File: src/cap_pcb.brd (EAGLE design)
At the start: 36 x 80 mm, 8 parts, among them CON1 PINHEAD_2X02-PTH-2-MALE, CON6 PINHEAD_2X02-PTH-2-MALE

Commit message: Updates here and there
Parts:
- removed CON6: PINHEAD_2X02-PTH-2-MALE, pinhead:2X02-PTH-2
- added CON2, CON3, CON4: PINHEAD_2X02-PTH-2-MALE, pinhead:2X02-PTH-2
- C17, C18, C19, C20, C21, C23: value 100µF -> 330µF
- moved C18 28.3 mm to (-8.75, 23.4), turned to 180 degrees
- moved C19 28.3 mm to (8.75, 23.4), turned to 180 degrees
- moved C20 22.5 mm to (-8.75, 47.9), turned to 180 degrees
- moved C21 22.5 mm to (8.75, 47.9), turned to 180 degrees
- moved CON1 1.00 mm to (15.7, 57.0)
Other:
- board size 36 x 80 mm -> 36 x 68 mm

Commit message: capacitor PCB polygons update
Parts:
- added PAD1, PAD2, PAD3, PAD4, PAD5, PAD6, PAD7, PAD8: PAD-5X4, PADS:5X4
- added U$1, U$2: (no value), logo:ZUBAX_25X12
- flipped C17 to the bottom
- flipped C23 to the bottom
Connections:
- net GND: now also CON3.1, CON3.2, CON3.3, CON3.4, CON4.1, CON4.2, CON4.3, CON4.4, PAD3.P$1, PAD6.P$1, PAD7.P$1, PAD8.P$1
- net VBAT: now also CON1.1, CON1.2, CON1.3, CON1.4, CON2.1, CON2.2, CON2.3, CON2.4, PAD1.P$1, PAD2.P$1, PAD4.P$1, PAD5.P$1
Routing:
- added copper zone on layer 16, net GND
- added copper zone on layer 1, net VBAT
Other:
- board size 36 x 68 mm -> 36 x 70 mm
- board text added: "GND"
- board text added: "VDC"

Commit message: Silkscreen updates
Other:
- board text added: "+"
- board text added: "-"
- board text added: "Valenok CAP PCB V0.1"
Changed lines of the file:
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@@
 <setting verticaltext="up"/>
 </settings>
-<grid distance="1" unitdist="mm" unit="mm" style="lines" multiple="1" display="yes" altdistance="5" altunitdist="mil" altunit="mil"/>
+<grid distance="0.5" unitdist="mm" unit="mm" style="lines" multiple="1" display="yes" altdistance="5" altunitdist="mil" altunit="mil"/>
 <layers>
 <layer number="1" name="Top" color="4" fill="1" visible="yes" active="yes"/>
@@
 </layers>
 <board>
-<fusionsync huburn="a.cGVyc29uYWw6dWUyYWE4ZDY4" projecturn="a.cGVyc29uYWw6dWUyYWE4ZDY4IzIwMjAwOTI1MzM2NDYxMjgx" f3durn="urn:adsk.wipprod:dm.lineage:IhySjAM5SyGK940RRZt57A" pcbguid="" lastpulledtime="" lastsyncedchangeguid="" latestrevisionid="afba331b-8359-4740-9163-e93e92381942" lastsyncedrevisionid="afba331b-8359-4740-9163-e93e92381942" lastboardhashguid="2d678b6d-4d74-7ef4-afec-71a2cf9df9c4" lastpushedtime="2020-10-31T23:32:12Z" linktopcb3d="true"/>
+<fusionsync huburn="a.cGVyc29uYWw6dWUyYWE4ZDY4" projecturn="a.cGVyc29uYWw6dWUyYWE4ZDY4IzIwMjAwOTI1MzM2NDYxMjgx" f3durn="urn:adsk.wipprod:dm.lineage:IhySjAM5SyGK940RRZt57A" pcbguid="" lastpulledtime="" lastsyncedchangeguid="" latestrevisionid="b7570ab4-b679-4fac-b5e5-818cc3172e16" lastsyncedrevisionid="b7570ab4-b679-4fac-b5e5-818cc3172e16" lastboardhashguid="ee9d795c-402e-5159-a8c4-1897fa97820f" lastpushedtime="2020-11-16T10:37:36Z" linktopcb3d="true"/>
 <plain>
 <wire x1="0" y1="0" x2="0" y2="80" width="0.01" layer="47" style="shortdash" locked="yes"/>
@@
 <text x="15" y="18" size="2" layer="22" font="vector" ratio="15" rot="MR0" align="center">VDC</text>
 <text x="-15" y="18" size="2" layer="22" font="vector" ratio="15" rot="MR0" align="center">GND</text>
+<text x="-16" y="38" size="2.3" layer="21" font="vector" ratio="15" rot="R90" align="center">Valenok CAP PCB V0.1</text>
+<text x="-5" y="51" size="2.3" layer="21" font="vector" ratio="15" align="center">+</text>
+<text x="-5" y="49" size="2.3" layer="21" font="vector" ratio="15" align="center">+</text>
+<text x="13" y="50" size="2.3" layer="21" font="vector" ratio="15" align="center">+</text>
+<text x="13" y="48" size="2.3" layer="21" font="vector" ratio="15" align="center">+</text>
+<text x="13" y="23.5" size="2.3" layer="21" font="vector" ratio="15" align="center">+</text>
+<text x="-4.5" y="23.5" size="2.3" layer="21" font="vector" ratio="15" align="center">+</text>
+<text x="-9.5" y="51.5" size="2.3" layer="21" font="vector" ratio="15" align="center">-</text>
+<text x="-9.5" y="49.5" size="2.3" layer="21" font="vector" ratio="15" align="center">-</text>
+<text x="4.5" y="51" size="2.3" layer="21" font="vector" ratio="15" align="center">-</text>
+<text x="4.5" y="49" size="2.3" layer="21" font="vector" ratio="15" align="center">-</text>
+<text x="4" y="23.5" size="2.3" layer="21" font="vector" ratio="15" align="center">-</text>
+<text x="-13.5" y="23.5" size="2.3" layer="21" font="vector" ratio="15" align="center">-</text>
 </plain>
 <attributes>

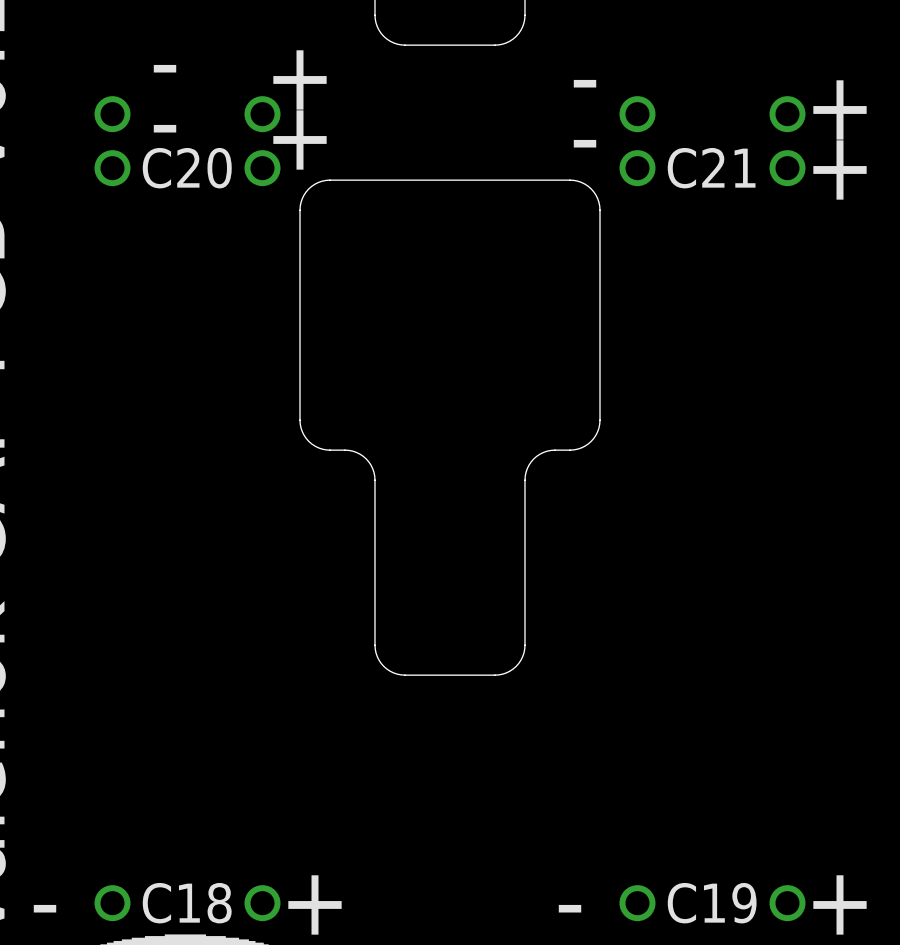
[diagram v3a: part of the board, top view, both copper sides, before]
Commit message: Interpcb connectors updated. Ground problem solved
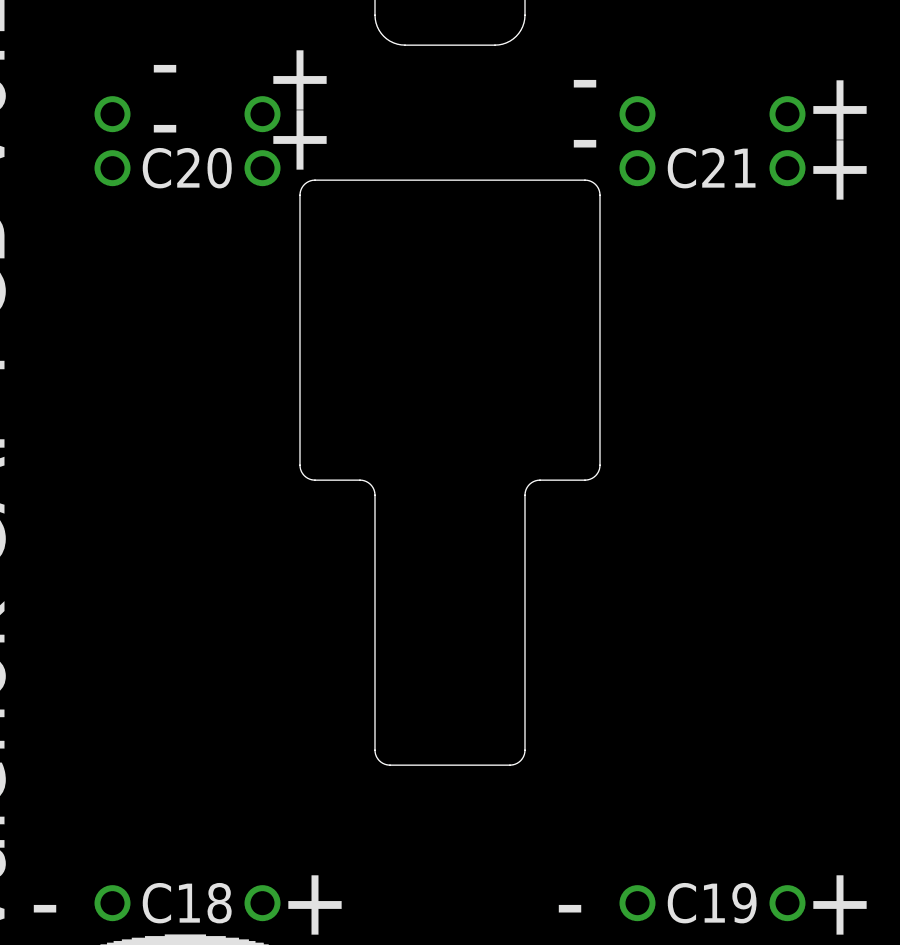
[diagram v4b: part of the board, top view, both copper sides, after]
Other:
- outline, holes or cut-outs redrawn
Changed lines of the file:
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@@
 <setting verticaltext="up"/>
 </settings>
-<grid distance="0.5" unitdist="mm" unit="mm" style="lines" multiple="1" display="yes" altdistance="5" altunitdist="mil" altunit="mil"/>
+<grid distance="3" unitdist="mm" unit="mm" style="lines" multiple="1" display="yes" altdistance="5" altunitdist="mil" altunit="mil"/>
 <layers>
 <layer number="1" name="Top" color="4" fill="1" visible="yes" active="yes"/>
@@
 </layers>
 <board>
-<fusionsync huburn="a.cGVyc29uYWw6dWUyYWE4ZDY4" projecturn="a.cGVyc29uYWw6dWUyYWE4ZDY4IzIwMjAwOTI1MzM2NDYxMjgx" f3durn="urn:adsk.wipprod:dm.lineage:IhySjAM5SyGK940RRZt57A" pcbguid="" lastpulledtime="" lastsyncedchangeguid="" latestrevisionid="b7570ab4-b679-4fac-b5e5-818cc3172e16" lastsyncedrevisionid="b7570ab4-b679-4fac-b5e5-818cc3172e16" lastboardhashguid="ee9d795c-402e-5159-a8c4-1897fa97820f" lastpushedtime="2020-11-16T10:37:36Z" linktopcb3d="true"/>
+<fusionsync huburn="a.cGVyc29uYWw6dWUyYWE4ZDY4" projecturn="a.cGVyc29uYWw6dWUyYWE4ZDY4IzIwMjAwOTI1MzM2NDYxMjgx" f3durn="urn:adsk.wipprod:dm.lineage:IhySjAM5SyGK940RRZt57A" pcbguid="" lastpulledtime="" lastsyncedchangeguid="" latestrevisionid="58f9f851-a586-4f26-860e-32dd1fdea93e" lastsyncedrevisionid="58f9f851-a586-4f26-860e-32dd1fdea93e" lastboardhashguid="95444913-4099-2608-243f-9d9163b8668c" lastpushedtime="2020-11-20T12:15:10Z" linktopcb3d="true"/>
 <plain>
 <wire x1="0" y1="0" x2="0" y2="80" width="0.01" layer="47" style="shortdash" locked="yes"/>
@@
 <rectangle x1="-2.5" y1="10" x2="2.5" y2="18" layer="49"/>
 <wire x1="-1.5" y1="10" x2="1.5" y2="10" width="0.01" layer="20"/>
-<wire x1="5" y1="39.5" x2="5" y2="46.5" width="0.01" layer="20"/>
-<wire x1="5" y1="46.5" x2="4" y2="47.5" width="0.01" layer="20" curve="90"/>
-<wire x1="4" y1="47.5" x2="-4" y2="47.5" width="0.01" layer="20"/>
-<wire x1="-4" y1="47.5" x2="-5" y2="46.5" width="0.01" layer="20" curve="90"/>
-<wire x1="-5" y1="46.5" x2="-5" y2="39.5" width="0.01" layer="20"/>
-<wire x1="-1.5" y1="31" x2="1.5" y2="31" width="0.01" layer="20"/>
-<wire x1="1.5" y1="31" x2="2.5" y2="32" width="0.01" layer="20" curve="90"/>
-<wire x1="2.5" y1="32" x2="2.5" y2="37.5" width="0.01" layer="20"/>
-<wire x1="2.5" y1="37.5" x2="3.5" y2="38.5" width="0.01" layer="20" curve="-90"/>
-<wire x1="3.5" y1="38.5" x2="4" y2="38.5" width="0.01" layer="20"/>
-<wire x1="-2.5" y1="37.5" x2="-2.5" y2="32" width="0.01" layer="20"/>
-<wire x1="-2.5" y1="32" x2="-1.5" y2="31" width="0.01" layer="20" curve="90"/>
-<wire x1="-4" y1="38.5" x2="-3.5" y2="38.5" width="0.01" layer="20"/>
-<wire x1="-3.5" y1="38.5" x2="-2.5" y2="37.5" width="0.01" layer="20" curve="-90"/>
-<wire x1="-5" y1="39.5" x2="-4" y2="38.5" width="0.01" layer="20" curve="90"/>
-<wire x1="4" y1="38.5" x2="5" y2="39.5" width="0.01" layer="20" curve="90"/>
+<wire x1="-2.5" y1="37" x2="-2.5" y2="28.5" width="0.01" layer="20"/>
+<wire x1="-2.5" y1="28.5" x2="-2" y2="28" width="0.01" layer="20" curve="90"/>
+<wire x1="-2" y1="28" x2="2" y2="28" width="0.01" layer="20"/>
+<wire x1="2" y1="28" x2="2.5" y2="28.5" width="0.01" layer="20" curve="90"/>
+<wire x1="2.5" y1="28.5" x2="2.5" y2="37" width="0.01" layer="20"/>
+<wire x1="2.5" y1="37" x2="3" y2="37.5" width="0.01" layer="20" curve="-90"/>
+<wire x1="3" y1="37.5" x2="4.5" y2="37.5" width="0.01" layer="20"/>
+<wire x1="4.5" y1="37.5" x2="5" y2="38" width="0.01" layer="20" curve="90"/>
+<wire x1="5" y1="38" x2="5" y2="47" width="0.01" layer="20"/>
+<wire x1="5" y1="47" x2="4.5" y2="47.5" width="0.01" layer="20" curve="90"/>
+<wire x1="4.5" y1="47.5" x2="-4.5" y2="47.5" width="0.01" layer="20"/>
+<wire x1="-4.5" y1="47.5" x2="-5" y2="47" width="0.01" layer="20" curve="90"/>
+<wire x1="-5" y1="47" x2="-5" y2="38" width="0.01" layer="20"/>
+<wire x1="-5" y1="38" x2="-4.5" y2="37.5" width="0.01" layer="20" curve="90"/>
+<wire x1="-4.5" y1="37.5" x2="-3" y2="37.5" width="0.01" layer="20"/>
+<wire x1="-3" y1="37.5" x2="-2.5" y2="37" width="0.01" layer="20" curve="-90"/>
 <wire x1="-1.5" y1="60" x2="1.5" y2="60" width="0.01" layer="20"/>
 <wire x1="1.5" y1="60" x2="2.5" y2="59" width="0.01" layer="20" curve="-90"/>
